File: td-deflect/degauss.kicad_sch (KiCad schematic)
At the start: 9 parts, among them J12 Conn_01x02_Male, Q22 IPD50R380CE, U38 MCP1416

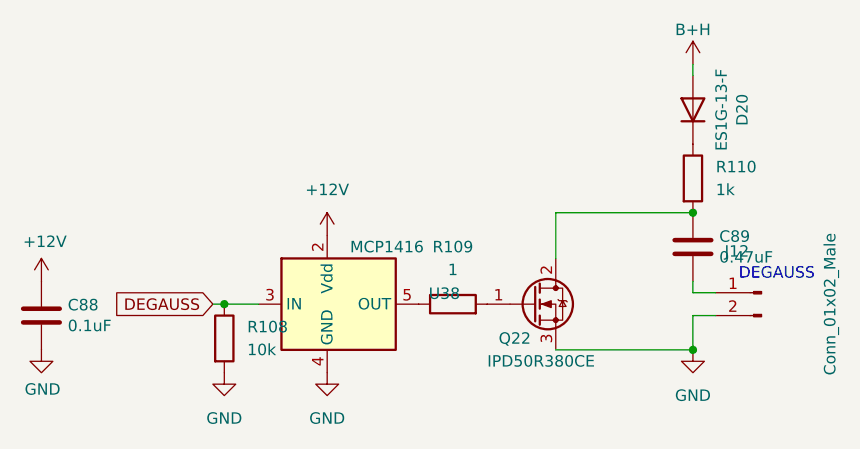
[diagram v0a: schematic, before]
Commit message: shrink board a lot
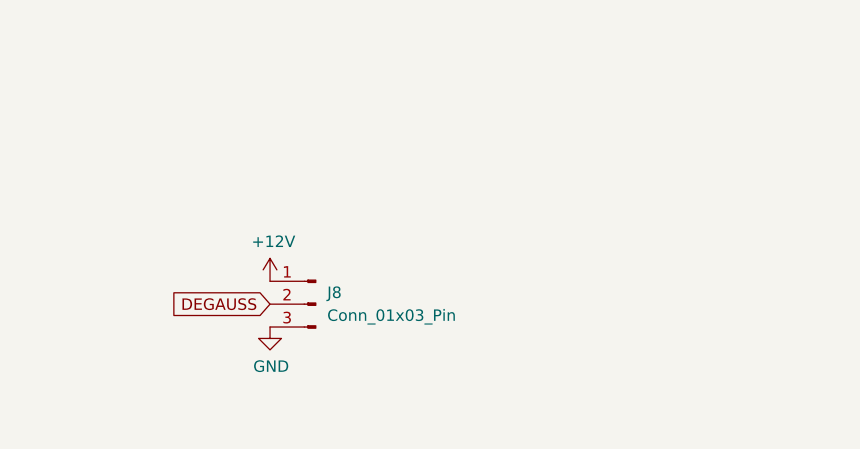
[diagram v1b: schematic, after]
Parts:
- removed C88: 0.1uF, Capacitor_SMD:C_0805_2012Metric_Pad1.18x1.45mm_HandSolder, symbol Device:C
- removed C89: 0.47uF, Capacitor_THT:C_Rect_L18.0mm_W8.0mm_P15.00mm_FKS3_FKP3, symbol Device:C
- removed D20: ES1G-13-F, Diode_SMD:D_SMA, symbol Diode:BA157
- removed J12: Conn_01x02_Male, td-deflect:monitor_10_8_2p, symbol Connector:Conn_01x02_Pin
- removed Q22: IPD50R380CE, Package_TO_SOT_SMD:TO-252-2, symbol Transistor_FET:IPD50R380CE
- removed R108: 10k, Resistor_SMD:R_0805_2012Metric_Pad1.20x1.40mm_HandSolder, symbol Device:R
- removed R109: 1, Resistor_SMD:R_0805_2012Metric_Pad1.20x1.40mm_HandSolder, symbol Device:R
- removed R110: 1k, Resistor_THT:R_Radial_Power_L13.0mm_W9.0mm_P5.00mm, symbol Device:R
- removed U38: MCP1416, Package_TO_SOT_SMD:SOT-23-5, symbol Driver_FET:MCP1416
- added J8: Conn_01x03_Pin, symbol Connector:Conn_01x03_Pin
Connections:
- net +12V: now also J8.1 (Pin_1)
- net DEGAUSS: now also J8.2 (Pin_2)
- net GND: now also J8.3 (Pin_3)
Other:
- note removed: "DEGAUSS"

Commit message: finish board
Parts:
- J8: footprint (none) -> Connector_JST:JST_XH_B3B-XH-A_1x03_P2.50mm_Vertical
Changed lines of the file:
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@@
 			)
 		)
-		(property "Footprint" ""
+		(property "Footprint" "Connector_JST:JST_XH_B3B-XH-A_1x03_P2.50mm_Vertical"
 			(at 127 83.82 0)
 			(effects

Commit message: Update td-deflect to 0.3
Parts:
- J8: Digikey (none) -> 455-2248-ND
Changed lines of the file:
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@@
+			)
+		)
+		(property "Digikey" "455-2248-ND"
+			(at 127 83.82 0)
+			(effects
+				(font
+					(size 1.27 1.27)
+				)
+				(hide yes)
 			)
 		)
